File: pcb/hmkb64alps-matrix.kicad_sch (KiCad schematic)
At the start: 136 parts, among them SW1 SW_Push, SW10 SW_Push, SW11 SW_Push, SW12 SW_Push, SW13 SW_Push, SW14 SW_Push, SW15 SW_Push, SW16 SW_Push, SW17 SW_Push, SW18 SW_Push, SW19 SW_Push, SW2 SW_Push, SW20 SW_Push, SW21 SW_Push, SW22 SW_Push, SW23 SW_Push, SW24 SW_Push, SW25 SW_Push, SW26 SW_Push, SW27 SW_Push, SW28 SW_Push, SW29 SW_Push, SW3 SW_Push, SW30 SW_Push, SW31 SW_Push, SW32 SW_Push, SW33 SW_Push, SW34 SW_Push, SW35 SW_Push, SW36 SW_Push, SW37 SW_Push, SW38 SW_Push, SW39 SW_Push, SW4 SW_Push, SW40 SW_Push, SW41 SW_Push, SW42 SW_Push, SW43 SW_Push, SW44 SW_Push, SW45 SW_Push, SW46 SW_Push, SW47 SW_Push, SW48 SW_Push, SW49 SW_Push, SW5 SW_Push, SW50 SW_Push, SW51 SW_Push, SW52 SW_Push, SW53 SW_Push, SW54 SW_Push, SW55 SW_Push, SW56 SW_Push, SW57 SW_Push, SW58 SW_Push, SW59 SW_Push, SW6 SW_Push, SW60 SW_Push, SW61 SW_Push, SW62 SW_Push, SW63 SW_Push, SW64 SW_Push, SW65 SW_Push, SW66 SW_Push, SW67 SW_Push, SW68 SW_Push, SW7 SW_Push, SW8 SW_Push, SW9 SW_Push

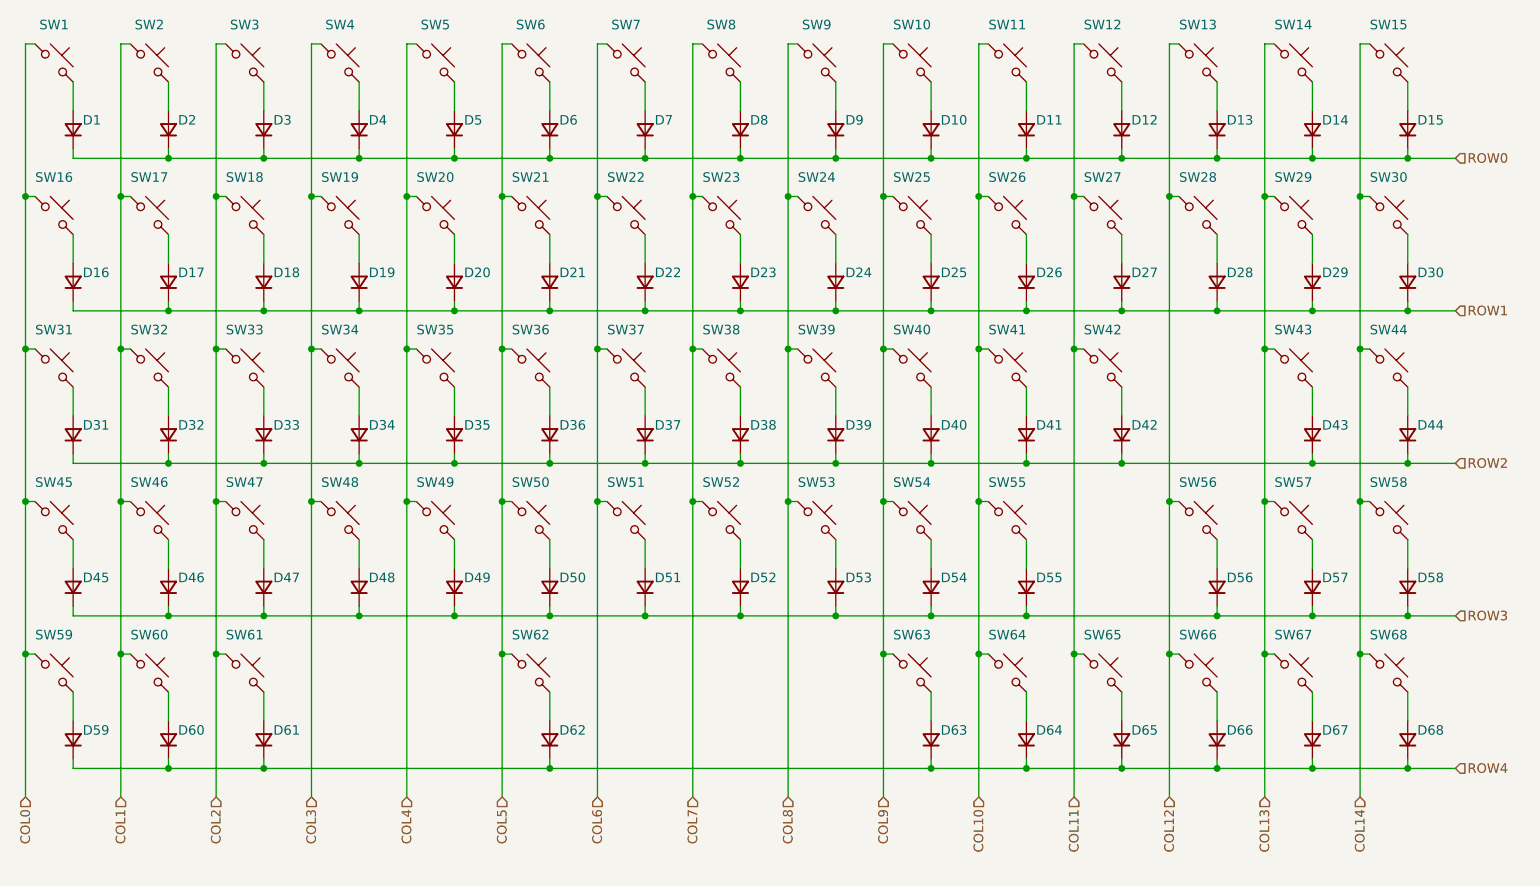
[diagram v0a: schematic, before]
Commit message: revert to global labels for matrix
kbplacer does unfortunately not seem to work with local or hierarchical
labels (which I would have prefered). So global labels it is.
Essentially that means using the schematic generated by
`layout2schematic.py` works fine and best.
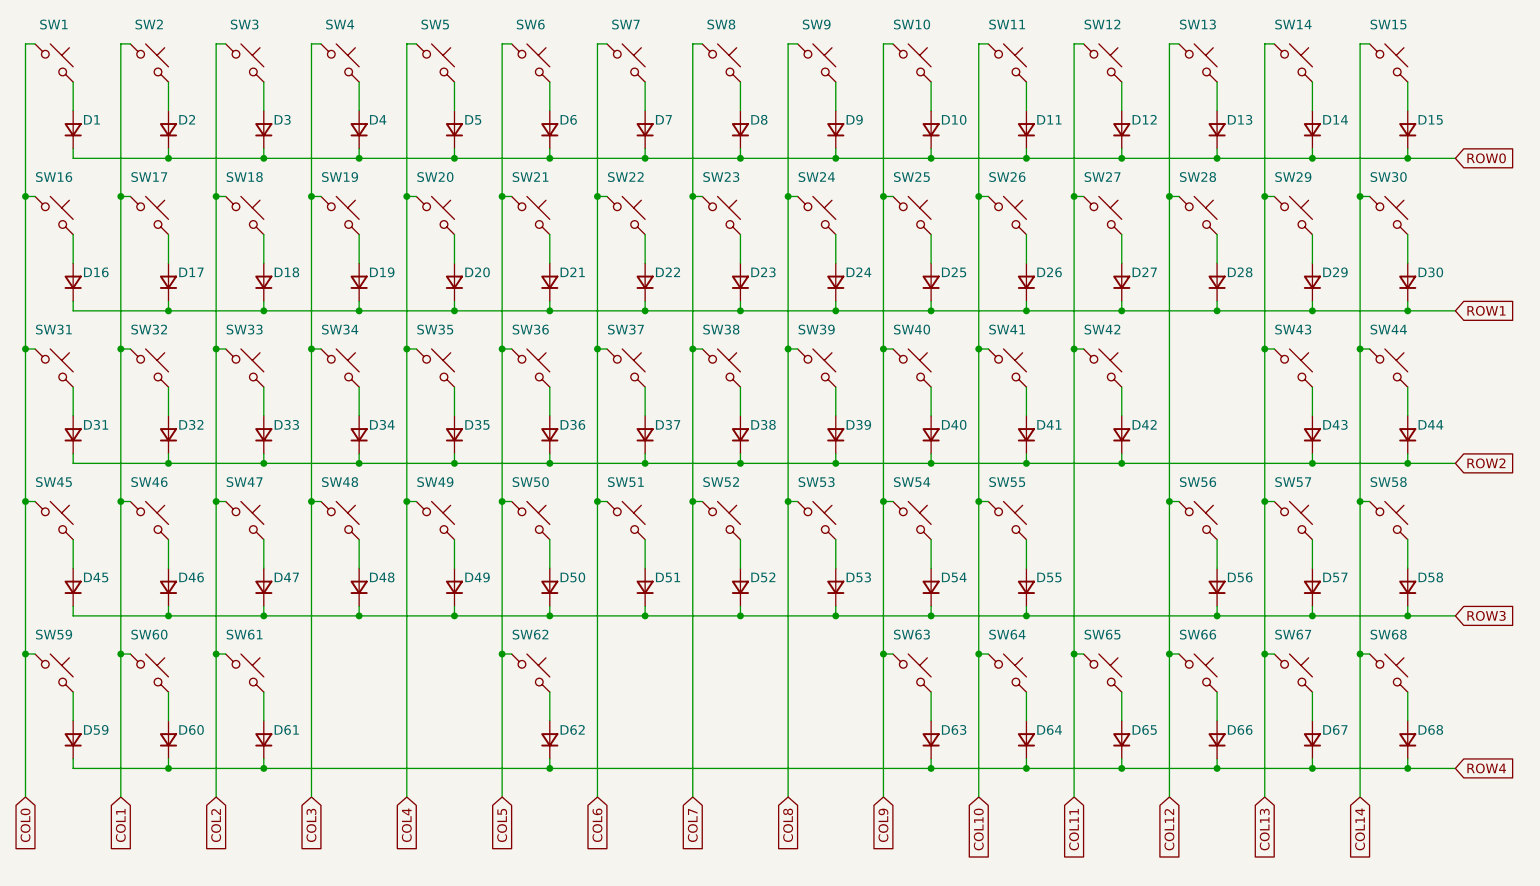
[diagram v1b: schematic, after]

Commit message: assign correct switch footprints to all switches
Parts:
- SW14: footprint MX_Alps_Hybrid:MX-Alps-Hybrid-1U -> MX_Alps_Hybrid:MX-Alps-Hybrid-2U
- SW16, SW29: footprint MX_Alps_Hybrid:MX-Alps-Hybrid-1U -> MX_Alps_Hybrid:MX-Alps-Hybrid-1.5U
- SW31, SW56: footprint MX_Alps_Hybrid:MX-Alps-Hybrid-1U -> MX_Alps_Hybrid:MX-Alps-Hybrid-1.75U
- SW43, SW45: footprint MX_Alps_Hybrid:MX-Alps-Hybrid-1U -> MX_Alps_Hybrid:MX-Alps-Hybrid-2.25U
- SW59, SW60, SW61: footprint MX_Alps_Hybrid:MX-Alps-Hybrid-1U -> MX_Alps_Hybrid:MX-Alps-Hybrid-1.25U
- SW62: footprint MX_Alps_Hybrid:MX-Alps-Hybrid-1U -> MX_Alps_Hybrid:MX-Alps-Hybrid-6.25U
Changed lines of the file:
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@@
 			)
 		)
-		(property "Footprint" "MX_Alps_Hybrid:MX-Alps-Hybrid-1U"
+		(property "Footprint" "MX_Alps_Hybrid:MX-Alps-Hybrid-6.25U"
 			(at 92.71 104.14 0)
 			(effects
@@
 			)
 		)
-		(property "Footprint" "MX_Alps_Hybrid:MX-Alps-Hybrid-1U"
+		(property "Footprint" "MX_Alps_Hybrid:MX-Alps-Hybrid-1.25U"
 			(at 41.91 104.14 0)
 			(effects
@@
 			)
 		)
-		(property "Footprint" "MX_Alps_Hybrid:MX-Alps-Hybrid-1U"
+		(property "Footprint" "MX_Alps_Hybrid:MX-Alps-Hybrid-1.75U"
 			(at 29.21 63.5 0)
 			(effects
@@
 			)
 		)
-		(property "Footprint" "MX_Alps_Hybrid:MX-Alps-Hybrid-1U"
+		(property "Footprint" "MX_Alps_Hybrid:MX-Alps-Hybrid-1.75U"
 			(at 181.61 83.82 0)
 			(effects
@@
 			)
 		)
-		(property "Footprint" "MX_Alps_Hybrid:MX-Alps-Hybrid-1U"
+		(property "Footprint" "MX_Alps_Hybrid:MX-Alps-Hybrid-2.25U"
 			(at 29.21 83.82 0)
 			(effects
@@
 			)
 		)
-		(property "Footprint" "MX_Alps_Hybrid:MX-Alps-Hybrid-1U"
+		(property "Footprint" "MX_Alps_Hybrid:MX-Alps-Hybrid-1.25U"
 			(at 54.61 104.14 0)
 			(effects
@@
 			)
 		)
-		(property "Footprint" "MX_Alps_Hybrid:MX-Alps-Hybrid-1U"
+		(property "Footprint" "MX_Alps_Hybrid:MX-Alps-Hybrid-1.5U"
 			(at 29.21 43.18 0)
 			(effects
@@
 			)
 		)
-		(property "Footprint" "MX_Alps_Hybrid:MX-Alps-Hybrid-1U"
+		(property "Footprint" "MX_Alps_Hybrid:MX-Alps-Hybrid-1.5U"
 			(at 194.31 43.18 0)
 			(effects
@@
 			)
 		)
-		(property "Footprint" "MX_Alps_Hybrid:MX-Alps-Hybrid-1U"
+		(property "Footprint" "MX_Alps_Hybrid:MX-Alps-Hybrid-2U"
 			(at 194.31 22.86 0)
 			(effects
@@
 			)
 		)
-		(property "Footprint" "MX_Alps_Hybrid:MX-Alps-Hybrid-1U"
+		(property "Footprint" "MX_Alps_Hybrid:MX-Alps-Hybrid-1.25U"
 			(at 29.21 104.14 0)
 			(effects
@@
 			)
 		)
-		(property "Footprint" "MX_Alps_Hybrid:MX-Alps-Hybrid-1U"
+		(property "Footprint" "MX_Alps_Hybrid:MX-Alps-Hybrid-2.25U"
 			(at 194.31 63.5 0)
 			(effects
